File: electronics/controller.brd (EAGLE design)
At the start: 100 x 80 mm, 9 parts, among them IC2 L293D

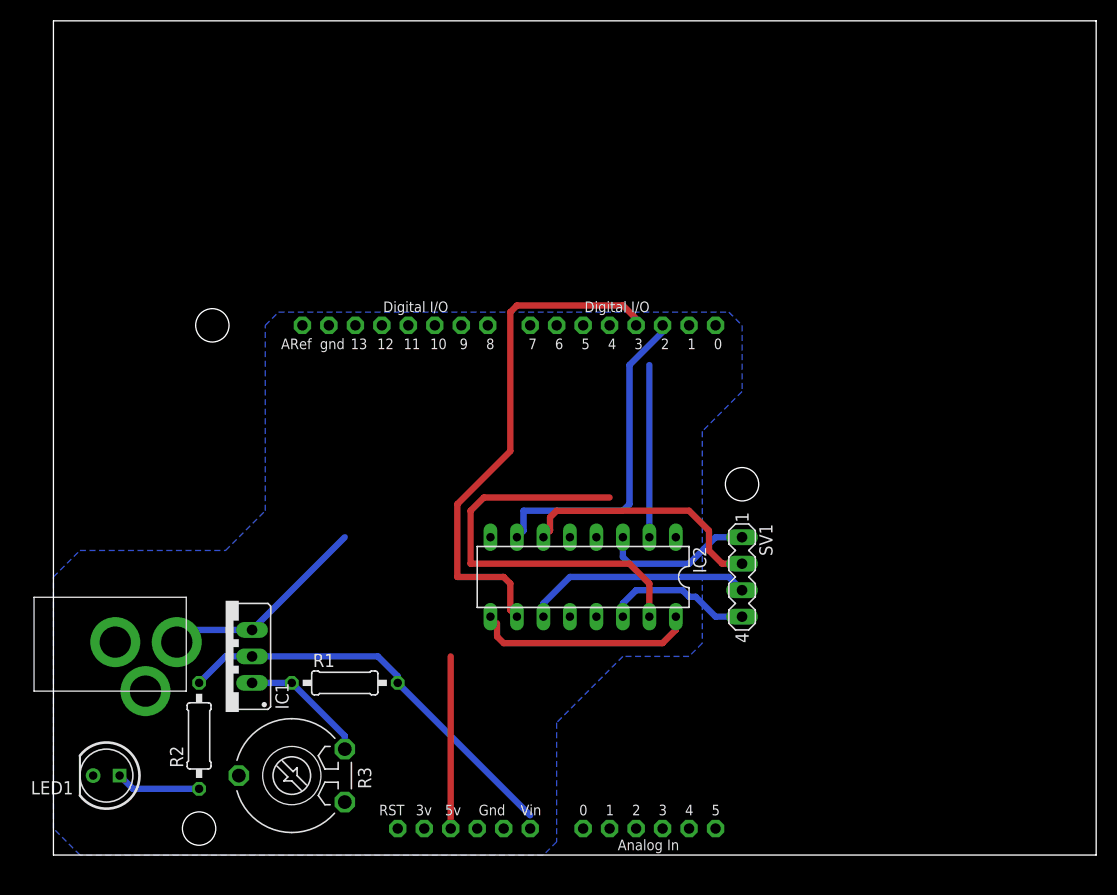
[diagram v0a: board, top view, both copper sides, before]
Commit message: Updated #robogarden manual control code and schematic
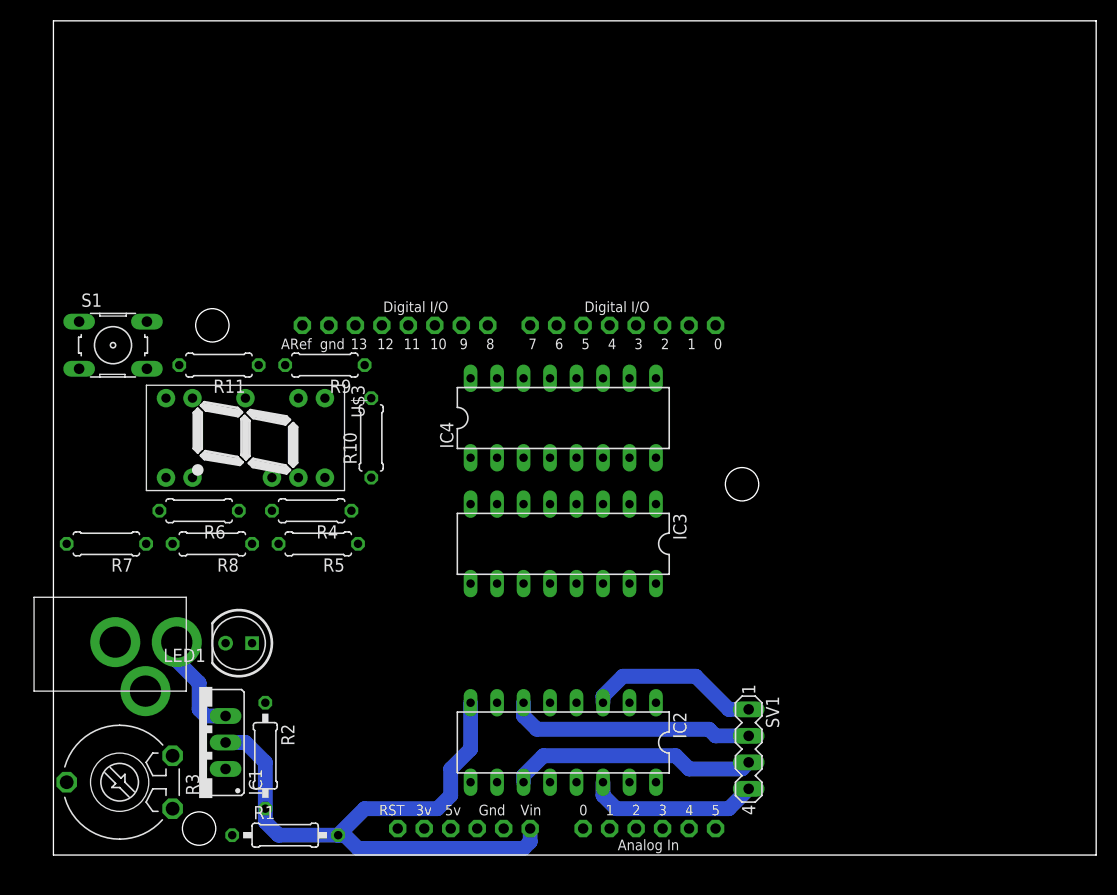
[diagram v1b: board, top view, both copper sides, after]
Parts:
- added IC3: 4511N, 45xx:DIL16
- added IC4: 74HC595N, 74xx-eu:DIL16
- added R10, R4, R5, R6, R7, R8, R9: 220, adafruit:0207/7
- added R11: 10K, adafruit:0207/7
- added S1: (no value), switch-omron:B3F-10XX
- added U$3: ELS-321HDB, national-semiconductor:ELS-321HDB
- moved LED1 18.0 mm to (17.8, 20.3)
- moved SV1 16.5 mm to (66.7, 10.2)
- moved R3 16.5 mm to (6.35, 6.99)
- moved IC2 16.0 mm to (48.9, 10.8)
- moved R1 15.7 mm to (22.2, 1.91)
- moved IC1 8.64 mm to (14.0, 10.8)
- moved R2 6.63 mm to (20.3, 9.53), turned to 270 degrees
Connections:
- new net N$13: IC2.1, IC2.9, U$1.D7
- new net N$14: IC3.11, R6.1
- new net N$15: IC3.10, R7.1
- new net N$16: IC3.9, R8.1
- new net N$17: IC3.15, R9.1
- new net N$18: IC3.14, R10.1
- new net N$19: R4.2, U$3.14
- new net N$20: R5.2, U$3.13
- new net N$21: R6.2, U$3.8
- new net N$22: R7.2, U$3.7
- new net N$23: R8.2, U$3.6
- new net N$24: R9.2, U$3.1
- new net N$25: R10.2, U$3.2
- new net N$26: IC3.7, IC4.15
- new net N$27: IC3.1, IC4.1
- new net N$28: IC3.2, IC4.2
- new net N$29: IC3.6, IC4.3
- new net N$30: IC4.14, U$1.D4
- new net N$31: IC4.11, U$1.D5
- new net N$32: IC4.12, U$1.D6
- new net N$34: R11.2, S1.4, U$1.D3
- net +5V: now also IC3.16, IC3.3, IC3.4, IC4.10, IC4.16, S1.2
- net GND: now also IC3.5, IC3.8, IC4.13, IC4.8, R11.1, U$3.4
- net N$12: now also IC3.12, R5.1; no longer IC2.1, IC2.9
- net N$2: now also IC3.13, R4.1; no longer IC1.2, R1.2, R2.2
- net V+: now also IC1.2, R1.2, R2.2
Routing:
- net V+: track 0.00 -> 60.4 mm
- net N$10: track 49.1 -> 0.00 mm
- net N$11: track 40.1 -> 0.00 mm
- net N$2: track 39.5 -> 0.00 mm
- net +5V: track 37.0 -> 0.00 mm
- net N$9: track 31.1 -> 0.00 mm
- net N$8: track 16.5 -> 0.00 mm
- net N$1: track 12.3 -> 0.00 mm
- net +12V: track 20.3 -> 10.1 mm
- net N$3: track 8.15 -> 0.00 mm
- net N$7: track 14.3 -> 16.6 mm
- net N$4: track 14.7 -> 16.7 mm
- net N$6: track 21.9 -> 23.8 mm
- removed copper zone on layer 16, net GND

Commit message: Updated #RoboGarden code with homing check, refactored the codebase to be cleaner with better comments and variable names, changed logic on button press
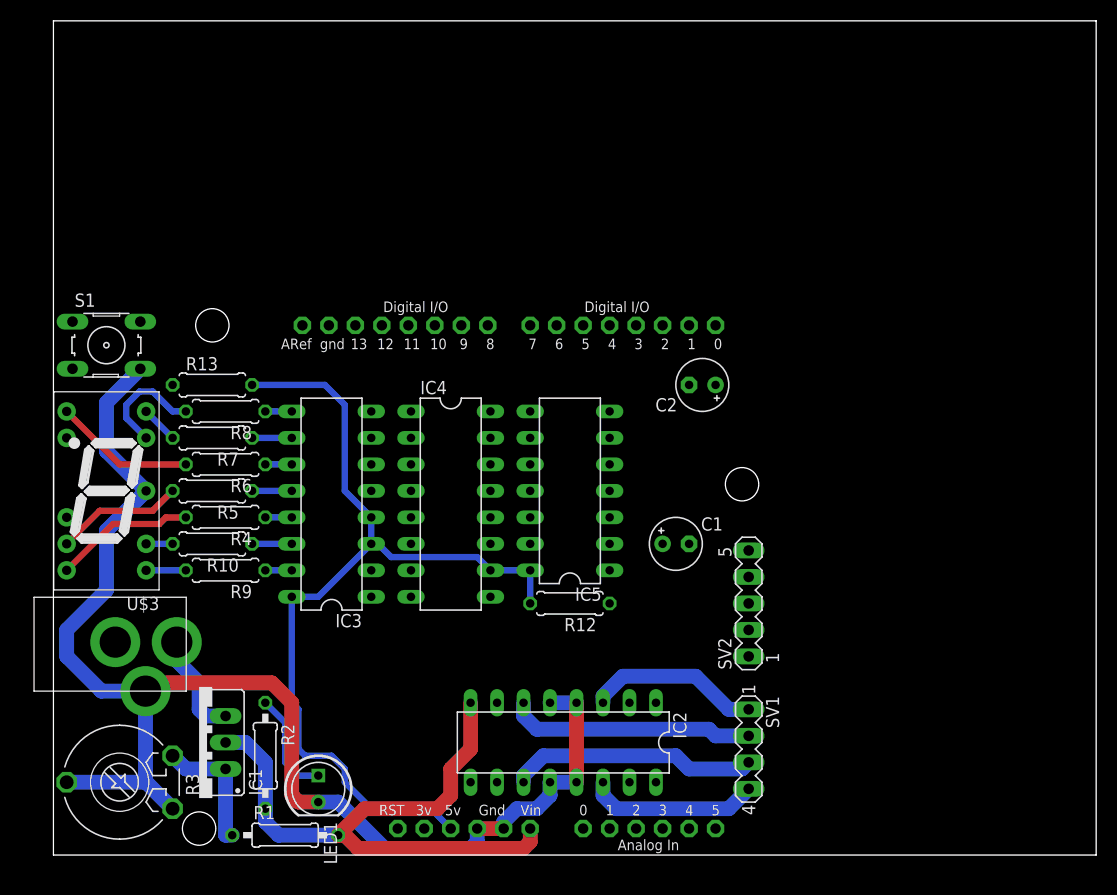
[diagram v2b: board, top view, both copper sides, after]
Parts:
- removed R11: 10K, adafruit:0207/7
- added C1, C2: 10uF, rcl:E2,5-5
- added IC5: 40106N, 40xx:DIL14
- added R12, R13: 10K, adafruit:0207/7
- added SV2: (no value), con-lstb:MA05-1
- moved IC3 22.5 mm to (26.7, 33.7), turned to 90 degrees
- moved R9 21.9 mm to (16.5, 27.3)
- moved R10 18.3 mm to (15.2, 29.8), turned to 180 degrees
- moved LED1 15.9 mm to (25.4, 6.35), turned to 270 degrees
- moved R7 14.4 mm to (15.2, 40.0)
- moved U$3 14.3 mm to (5.08, 34.9), turned to 180 degrees
- moved IC4 13.6 mm to (38.1, 33.7), turned to 270 degrees
- moved R8 12.8 mm to (16.5, 42.5)
- moved R5 11.4 mm to (15.2, 34.9)
- moved R4 8.28 mm to (16.5, 32.4)
- moved R6 5.12 mm to (16.5, 37.5)
- moved S1 0.63 mm to (5.08, 48.9)
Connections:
- new net N$33: C1.+, IC5.1, R13.1, S1.2
- new net N$35: C2.+, IC5.3, R12.1, SV2.2
- new net N$38: IC5.4, U$1.D2
- net +5V: now also IC5.14, R12.2, R13.2; no longer S1.2
- net GND: now also C1.-, C2.-, IC5.7, S1.4, SV2.1; no longer R11.1
- net N$34: now also IC5.2; no longer R11.2, S1.4
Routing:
- net GND: track 0.00 -> 134.3 mm
- net +5V: track 0.00 -> 86.6 mm
- net N$21: track 0.00 -> 13.5 mm
- net N$19: track 0.00 -> 13.5 mm
- net N$1: track 0.00 -> 12.6 mm
- net N$20: track 0.00 -> 12.3 mm
- net N$23: track 0.00 -> 11.0 mm
- net N$3: track 0.00 -> 10.2 mm
- net N$24: track 0.00 -> 3.81 mm
- net N$18: track 0.00 -> 3.81 mm
- net N$15: track 0.00 -> 3.81 mm
- net N$12: track 0.00 -> 3.81 mm
- net N$22: track 0.00 -> 3.59 mm
- net N$25: track 0.00 -> 2.54 mm
- net N$2: track 0.00 -> 2.54 mm
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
